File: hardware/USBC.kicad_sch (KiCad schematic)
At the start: 11 parts, among them J20 USB_C_Receptacle_USB2.0_16P, U33 USBLC6-2P6, U8 CP2102N-A02-GQFN20

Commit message: simple changes to the Pulse leds
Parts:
- added D13, D14: LED, LED_SMD:LED_0805_2012Metric, symbol Device:LED
- added R24, R25: 220, symbol Device:R
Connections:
- net GND: now also R24.1, R25.2
- net RXT: now reaches U8.19 (GPIO.3_/_RXT)
- net RXT: now also D14.2 (A)
- net TXT: now reaches U8.20 (GPIO.2_/_TXT)
- net TXT: now also D13.2 (A)
- new net: D14.1 (K), R25.1
- new net: D13.1 (K), R24.2
- no-connect marks 12 -> 10

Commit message: usbc-update
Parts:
- added U11: CDSOT236-0504C, Package_TO_SOT_SMD:SOT-23-6, symbol Power_Protection:CDSOT236-0504C
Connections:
- net 5V_VBUS: now also U11.5 (VP)
- net D_N: now also U11.6 (IO4)
- net D_P: now also U11.4 (IO3)
- net GND: now also U11.2 (VN)
- net CC_ONE: now reaches J20.A5 (CC1), R300.1
- net CC_ONE: now also U11.1 (IO1)
- net CC_TWO: now reaches J20.B5 (CC2), R9.1
- net CC_TWO: now also U11.3 (IO2)
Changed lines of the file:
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@@
+	(wire
+		(pts
+			(xy 99.06 128.27) (xy 102.87 128.27)
+		)
+		(stroke
+			(width 0)
+			(type default)
+		)
+	)
 	(wire
 		(pts
@@
 	(wire
 		(pts
+			(xy 102.87 128.27) (xy 102.87 134.62)
+		)
+		(stroke
+			(width 0)
+			(type default)
+		)
+	)
+	(wire
+		(pts
 			(xy 78.74 76.2) (xy 86.36 76.2)
 		)
@@
 	(wire
 		(pts
+			(xy 64.77 128.27) (xy 73.66 128.27)
+		)
+		(stroke
+			(width 0)
+			(type default)
+		)
+	)
+	(wire
+		(pts
 			(xy 77.47 91.44) (xy 77.47 88.9)
 		)
@@
 			(width 0)
 			(type default)
+		)
+	)
+	(label "CC_TWO"
+		(at 73.66 83.82 0)
+		(effects
+			(font
+				(size 1.27 1.27)
+			)
+			(justify left bottom)
 		)
 	)
@@
 		)
 	)
+	(label "CC_TWO"
+		(at 88.9 140.97 270)
+		(effects
+			(font
+				(size 1.27 1.27)
+			)
+			(justify right bottom)
+		)
+	)
 	(label "RXT"
 		(at 234.95 127 0)
@@
 	)
 	(label "D_N"
+		(at 88.9 115.57 0)
+		(effects
+			(font
+				(size 1.27 1.27)
+			)
+			(justify left bottom)
+		)
+	)
+	(label "D_N"
 		(at 105.41 68.58 180)
 		(effects
@@
 			)
 			(justify right bottom)
+		)
+	)
+	(label "CC_ONE"
+		(at 83.82 140.97 270)
+		(effects
+			(font
+				(size 1.27 1.27)
+			)
+			(justify right bottom)
+		)
+	)
+	(label "CC_ONE"
+		(at 73.66 81.28 0)
+		(effects
+			(font
+				(size 1.27 1.27)
+			)
+			(justify left bottom)
 		)
 	)
 	(label "D_P"
 		(at 73.66 93.98 0)
+		(effects
+			(font
+				(size 1.27 1.27)
+			)
+			(justify left bottom)
+		)
+	)
+	(label "D_P"
+		(at 83.82 115.57 0)
 		(effects
 			(font
@@
 		)
 	)
+	(hierarchical_label "5V_VBUS"
+		(shape output)
+		(at 64.77 128.27 180)
+		(effects
+			(font
+				(size 1.27 1.27)
+			)
+			(justify right)
+		)
+	)
 	(hierarchical_label "BUCK_3.3V"
 		(shape input)
@@
 	)
 	(symbol
+		(lib_id "Power_Protection:CDSOT236-0504C")
+		(at 86.36 128.27 90)
+		(unit 1)
+		(exclude_from_sim no)
+		(in_bom yes)
+		(on_board yes)
+		(dnp no)
+		(fields_autoplaced yes)
+		(property "Reference" "U11"
+			(at 106.68 121.8498 90)
+			(effects
+				(font
+					(size 1.27 1.27)
+				)
+			)
+		)
+		(property "Value" "CDSOT236-0504C"
+			(at 106.68 124.3898 90)
+			(effects
+				(font
+					(size 1.27 1.27)
+				)
+			)
+		)
+		(property "Footprint" "Package_TO_SOT_SMD:SOT-23-6"
+			(at 97.79 110.49 0)
+			(effects
+				(font
+					(size 1.27 1.27)
+				)
+				(hide yes)
+			)
+		)
+		(property "Datasheet" "https://www.bourns.com/docs/product-datasheets/cdsot236-0504c.pdf"
+			(at 86.36 128.27 0)
+			(effects
+				(font
+					(size 1.27 1.27)
+				)
+				(hide yes)
+			)
+		)
+		(property "Description" "Low capacitance ESD diode / steering Diode Array, SOT23-6"
+			(at 86.36 128.27 0)
+			(effects
+				(font
+					(size 1.27 1.27)
+				)
+				(hide yes)
+			)
+		)
+		(pin "3"
+		)
+		(pin "1"
+		)
+		(pin "4"
+		)
+		(pin "5"
+		)
+		(pin "2"
+		)
+		(pin "6"
+		)
+		(instances
+			(project ""
+				(path "/8f5928e8-0fc1-4443-a20f-3bfeb956761e/53a20cc4-87c9-41e2-9c0c-c30bc75df497"
+					(reference "U11")
+					(unit 1)
+				)
+			)
+		)
+	)
+	(symbol
 		(lib_id "Device:R")
 		(at 142.24 127 0)
@@
 					(unit 1)
 				)
+			)
+		)
+	)
+	(symbol
+		(lib_id "power:GND")
+		(at 102.87 134.62 0)
+		(unit 1)
+		(exclude_from_sim no)
+		(in_bom yes)
+		(on_board yes)
+		(dnp no)
+		(fields_autoplaced yes)
+		(property "Reference" "#PWR030"
+			(at 102.87 140.97 0)
+			(effects
+				(font
+					(size 1.27 1.27)
+				)
+				(hide yes)
+			)
+		)
+		(property "Value" "GND"
+			(at 102.87 139.7 0)
+			(effects
+				(font
+					(size 1.27 1.27)
+				)
+			)
+		)
+		(property "Footprint" ""
+			(at 102.87 134.62 0)
+			(effects
+				(font
+					(size 1.27 1.27)
+				)
+				(hide yes)
+			)
+		)
+		(property "Datasheet" ""
+			(at 102.87 134.62 0)
+			(effects
+				(font
+					(size 1.27 1.27)
+				)
+				(hide yes)
+			)
+		)
+		(property "Description" "Power symbol creates a global label with name \"GND\" , ground"
+			(at 102.87 134.62 0)
+			(effects
+				(font
+					(size 1.27 1.27)
+				)
+				(hide yes)
+			)
+		)
+		(pin "1"
+		)
+		(instances
+			(project ""
+				(path "/8f5928e8-0fc1-4443-a20f-3bfeb956761e/53a20cc4-87c9-41e2-9c0c-c30bc75df497"
+					(reference "#PWR030")
+					(unit 1)
+				)

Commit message: Debugging LED added
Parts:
- R14, R26, R27, R28, R300, R9: footprint Resistor_SMD:R_0603_1608Metric -> Resistor_SMD:R_0805_2012Metric
- R24, R25: footprint (none) -> Resistor_SMD:R_0805_2012Metric
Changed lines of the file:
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@@
 			)
 		)
-		(property "Footprint" ""
+		(property "Footprint" "Resistor_SMD:R_0805_2012Metric"
 			(at 233.172 142.24 90)
 			(effects
@@
 			)
 		)
-		(property "Footprint" "Resistor_SMD:R_0603_1608Metric"
+		(property "Footprint" "Resistor_SMD:R_0805_2012Metric"
 			(at 85.09 83.058 90)
 			(effects
@@
 			)
 		)
-		(property "Footprint" "Resistor_SMD:R_0603_1608Metric"
+		(property "Footprint" "Resistor_SMD:R_0805_2012Metric"
 			(at 154.432 116.84 90)
 			(effects
@@
 			)
 		)
-		(property "Footprint" "Resistor_SMD:R_0603_1608Metric"
+		(property "Footprint" "Resistor_SMD:R_0805_2012Metric"
 			(at 140.462 116.84 90)
 			(effects
@@
 			)
 		)
-		(property "Footprint" "Resistor_SMD:R_0603_1608Metric"
+		(property "Footprint" "Resistor_SMD:R_0805_2012Metric"
 			(at 85.09 85.598 90)
 			(effects
@@
 			)
 		)
-		(property "Footprint" ""
+		(property "Footprint" "Resistor_SMD:R_0805_2012Metric"
 			(at 227.838 142.24 90)
 			(effects
@@
 			)
 		)
-		(property "Footprint" "Resistor_SMD:R_0603_1608Metric"
+		(property "Footprint" "Resistor_SMD:R_0805_2012Metric"
 			(at 140.462 127 90)
 			(effects
@@
 			)
 		)
-		(property "Footprint" "Resistor_SMD:R_0603_1608Metric"
+		(property "Footprint" "Resistor_SMD:R_0805_2012Metric"
 			(at 47.752 116.84 90)
 			(effects

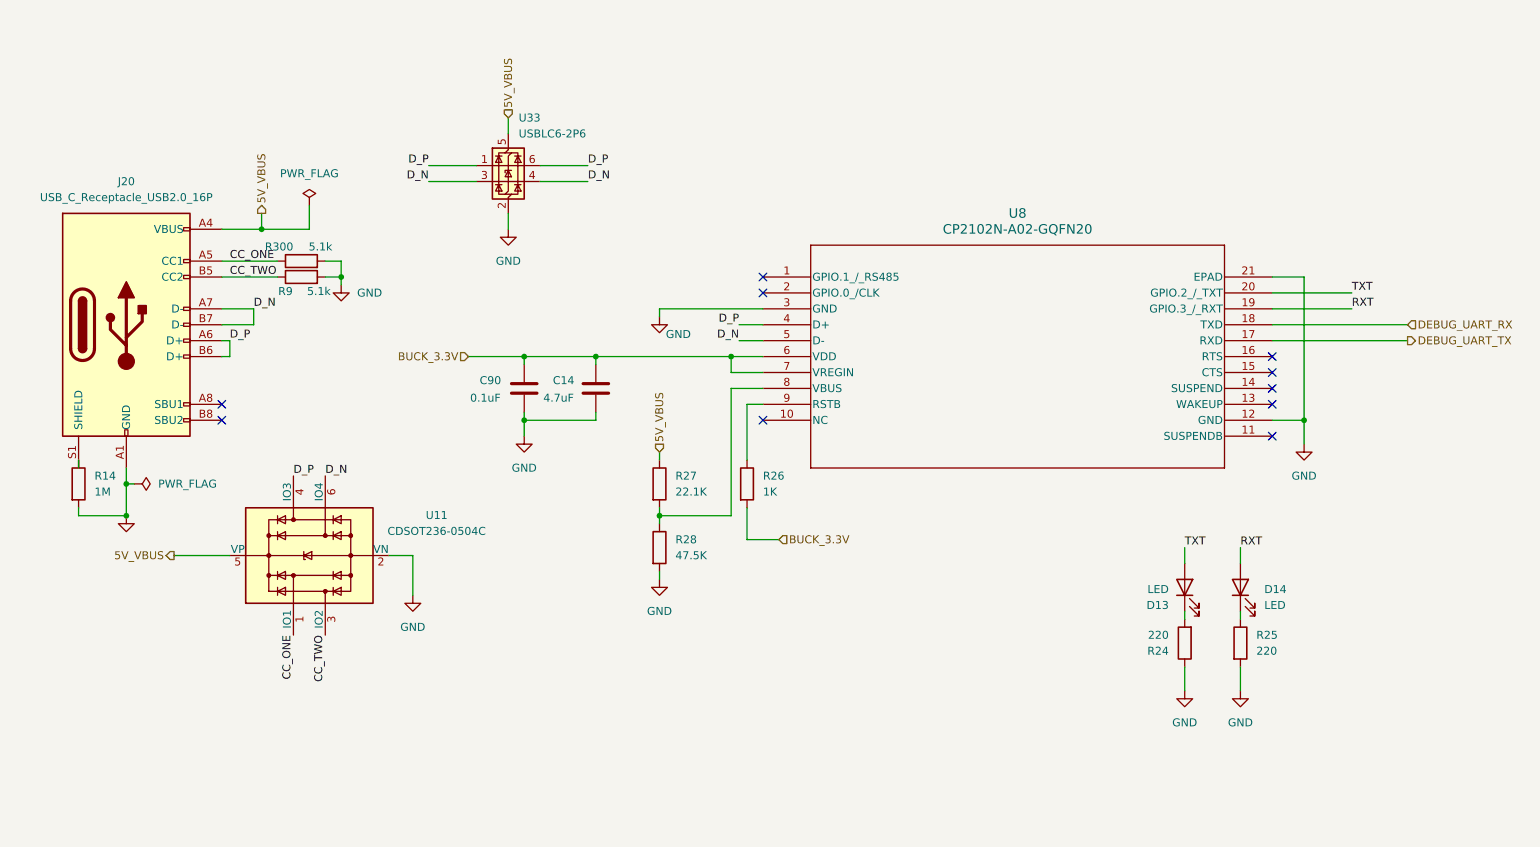
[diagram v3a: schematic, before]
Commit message: Fixed MCU JTAG/Reordered pages
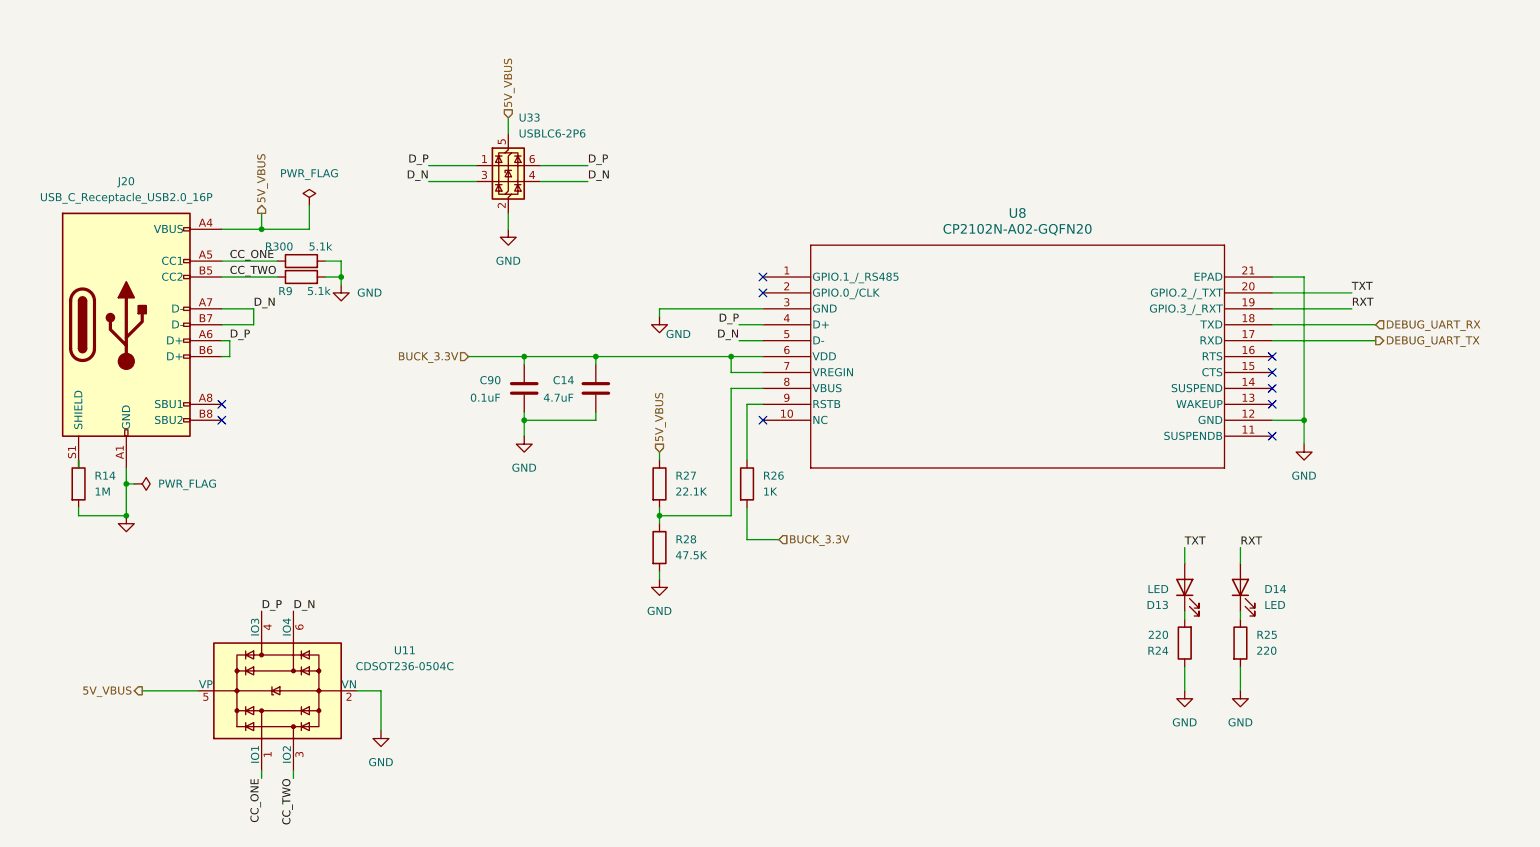
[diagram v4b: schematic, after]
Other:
- moved on the sheet: U11
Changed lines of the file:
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@@
+	(wire
+		(pts
+			(xy 78.74 163.83) (xy 78.74 162.56)
+		)
+		(stroke
+			(width 0)
+			(type default)
+		)
+	)
 	(wire
 		(pts
@@
 	(wire
 		(pts
-			(xy 240.03 91.44) (xy 261.62 91.44)
+			(xy 240.03 91.44) (xy 256.54 91.44)
 		)
 		(stroke
@@
 	(wire
 		(pts
-			(xy 240.03 93.98) (xy 261.62 93.98)
+			(xy 240.03 93.98) (xy 256.54 93.98)
 		)
 		(stroke
@@
 	(wire
 		(pts
-			(xy 99.06 128.27) (xy 102.87 128.27)
+			(xy 93.98 149.86) (xy 97.79 149.86)
 		)
 		(stroke
@@
 	(wire
 		(pts
-			(xy 102.87 128.27) (xy 102.87 134.62)
+			(xy 97.79 149.86) (xy 97.79 156.21)
 		)
 		(stroke
@@
 	(wire
 		(pts
+			(xy 83.82 163.83) (xy 83.82 162.56)
+		)
+		(stroke
+			(width 0)
+			(type default)
+		)
+	)
+	(wire
+		(pts
 			(xy 72.39 91.44) (xy 77.47 91.44)
 		)
@@
 	(wire
 		(pts
-			(xy 64.77 128.27) (xy 73.66 128.27)
+			(xy 59.69 149.86) (xy 68.58 149.86)
 		)
 		(stroke
@@
 	)
 	(label "CC_TWO"
-		(at 88.9 140.97 270)
+		(at 83.82 163.83 270)
 		(effects
 			(font
@@
 	)
 	(label "D_N"
-		(at 88.9 115.57 0)
+		(at 83.82 137.16 0)
 		(effects
 			(font
@@
 	)
 	(label "CC_ONE"
-		(at 83.82 140.97 270)
+		(at 78.74 163.83 270)
 		(effects
 			(font
@@
 	)
 	(label "D_P"
-		(at 83.82 115.57 0)
+		(at 78.74 137.16 0)
 		(effects
 			(font
@@
 	(hierarchical_label "DEBUG_UART_RX"
 		(shape input)
-		(at 261.62 91.44 0)
+		(at 256.54 91.44 0)
 		(effects
 			(font
@@
 	(hierarchical_label "DEBUG_UART_TX"
 		(shape output)
-		(at 261.62 93.98 0)
+		(at 256.54 93.98 0)
 		(effects
 			(font
@@
 	(hierarchical_label "5V_VBUS"
 		(shape output)
-		(at 64.77 128.27 180)
+		(at 59.69 149.86 180)
 		(effects
 			(font
@@
 	(symbol
 		(lib_id "Power_Protection:CDSOT236-0504C")
-		(at 86.36 128.27 90)
+		(at 81.28 149.86 90)
 		(unit 1)
 		(exclude_from_sim no)
@@
 		(fields_autoplaced yes)
 		(property "Reference" "U11"
-			(at 106.68 121.8498 90)
+			(at 101.6 143.4398 90)
 			(effects
 				(font
@@
 		)
 		(property "Value" "CDSOT236-0504C"
-			(at 106.68 124.3898 90)
+			(at 101.6 145.9798 90)
 			(effects
 				(font
@@
 		)
 		(property "Footprint" "Package_TO_SOT_SMD:SOT-23-6"
-			(at 97.79 110.49 0)
+			(at 92.71 132.08 0)
 			(effects
 				(font
@@
 		)
 		(property "Datasheet" "https://www.bourns.com/docs/product-datasheets/cdsot236-0504c.pdf"
-			(at 86.36 128.27 0)
+			(at 81.28 149.86 0)
 			(effects
 				(font
@@
 		)
 		(property "Description" "Low capacitance ESD diode / steering Diode Array, SOT23-6"
-			(at 86.36 128.27 0)
+			(at 81.28 149.86 0)
 			(effects
 				(font
@@
 	(symbol
 		(lib_id "power:GND")
-		(at 102.87 134.62 0)
+		(at 97.79 156.21 0)
 		(unit 1)
 		(exclude_from_sim no)
@@
 		(fields_autoplaced yes)
 		(property "Reference" "#PWR030"
-			(at 102.87 140.97 0)
+			(at 97.79 162.56 0)
 			(effects
 				(font
@@
 		)
 		(property "Value" "GND"
-			(at 102.87 139.7 0)
+			(at 97.79 161.29 0)
 			(effects
 				(font
@@
 		)
 		(property "Footprint" ""
-			(at 102.87 134.62 0)
+			(at 97.79 156.21 0)
 			(effects
 				(font
@@
 		)
 		(property "Datasheet" ""
-			(at 102.87 134.62 0)
+			(at 97.79 156.21 0)
 			(effects
 				(font
@@
 		)
 		(property "Description" "Power symbol creates a global label with name \"GND\" , ground"
-			(at 102.87 134.62 0)
-			(effects
-				(font
+			(at 97.79 156.21 0)
+			(effects
+				(font

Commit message: cleanup
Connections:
- net CC_ONE renamed CC1
- net CC_TWO renamed CC2
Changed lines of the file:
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@@
 		)
 	)
-	(label "CC_TWO"
+	(label "CC2"
 		(at 73.66 83.82 0)
 		(effects
@@
 		)
 	)
-	(label "CC_TWO"
+	(label "CC2"
 		(at 83.82 163.83 270)
 		(effects
@@
 		)
 	)
-	(label "CC_ONE"
+	(label "CC1"
 		(at 78.74 163.83 270)
 		(effects
@@
 		)
 	)
-	(label "CC_ONE"
+	(label "CC1"
 		(at 73.66 81.28 0)
 		(effects
@@
 		(dnp no)
 		(property "Reference" "R300"
-			(at 81.534 78.994 90)
-			(effects
-				(font
+			(at 82.55 78.486 90)
+			(effects
+				(font

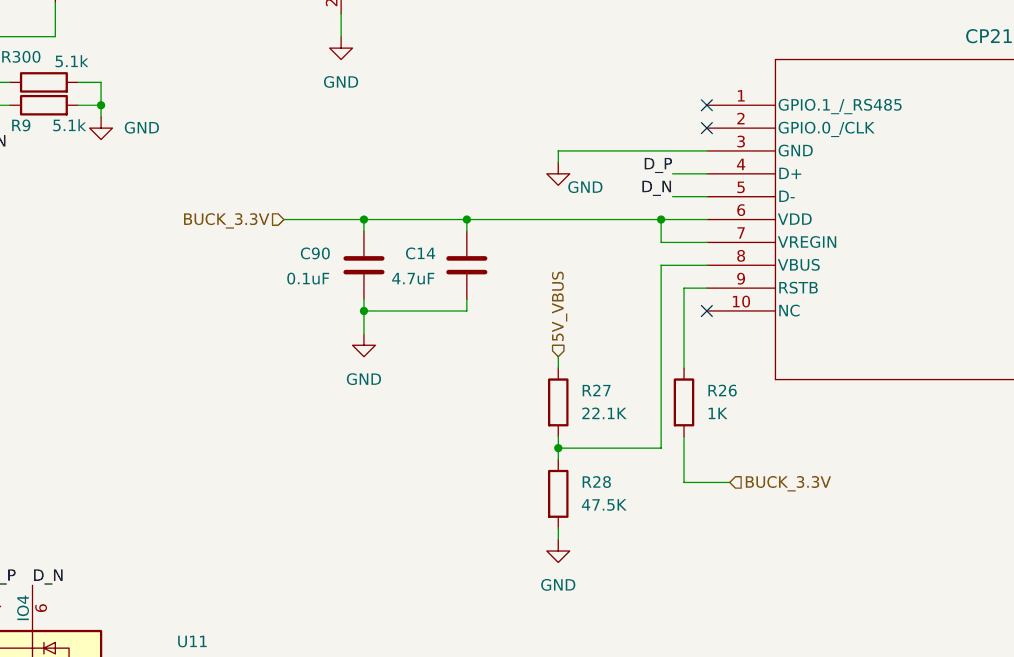
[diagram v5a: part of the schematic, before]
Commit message: Replaced 3.3V symbol
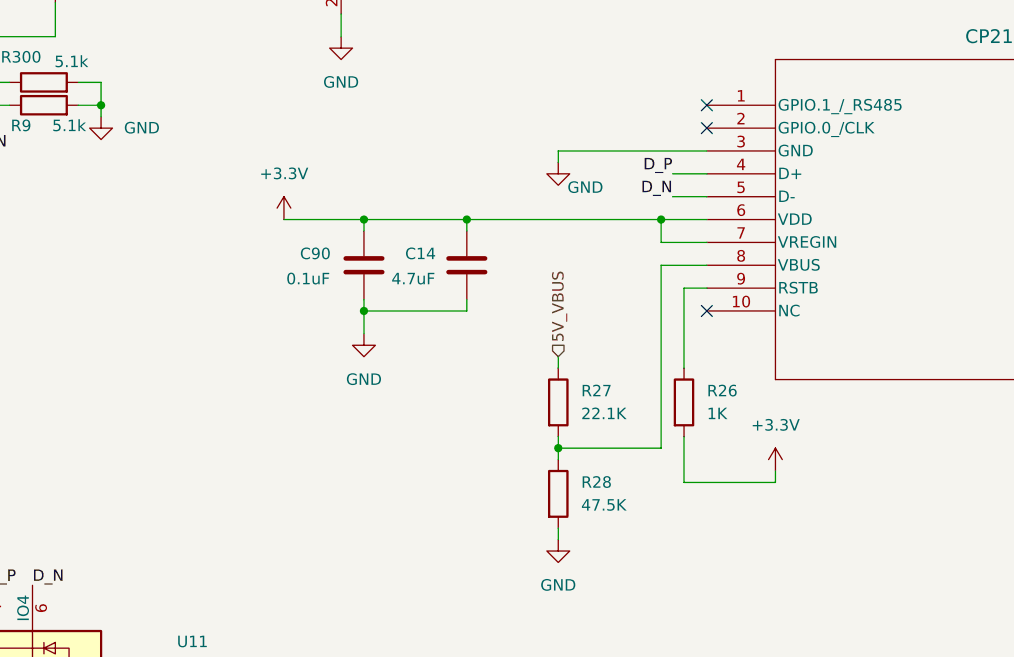
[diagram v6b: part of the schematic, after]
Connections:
- net BUCK_3.3V renamed +3.3V
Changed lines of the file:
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@@
 	(wire
 		(pts
-			(xy 156.21 125.73) (xy 161.29 125.73)
+			(xy 156.21 125.73) (xy 166.37 125.73)
 		)
 		(stroke
@@
 		(pts
 			(xy 240.03 93.98) (xy 256.54 93.98)
+		)
+		(stroke
+			(width 0)
+			(type default)
+		)
+	)
+	(wire
+		(pts
+			(xy 166.37 125.73) (xy 166.37 124.46)
 		)
 		(stroke
@@
 			)
 			(justify right bottom)
-		)
-	)
-	(hierarchical_label "BUCK_3.3V"
-		(shape input)
-		(at 161.29 125.73 0)
-		(effects
-			(font
-				(size 1.27 1.27)
-			)
-			(justify left)
 		)
 	)
@@
 		)
 	)
-	(hierarchical_label "BUCK_3.3V"
-		(shape input)
-		(at 111.76 96.52 180)
-		(effects
-			(font
-				(size 1.27 1.27)
-			)
-			(justify right)
-		)
-	)
 	(hierarchical_label "5V_VBUS"
 		(shape input)
@@
 	)
 	(symbol
+		(lib_id "power:+3.3V")
+		(at 111.76 96.52 0)
+		(unit 1)
+		(exclude_from_sim no)
+		(in_bom yes)
+		(on_board yes)
+		(dnp no)
+		(fields_autoplaced yes)
+		(property "Reference" "#PWR079"
+			(at 111.76 100.33 0)
+			(effects
+				(font
+					(size 1.27 1.27)
+				)
+				(hide yes)
+			)
+		)
+		(property "Value" "+3.3V"
+			(at 111.76 91.44 0)
+			(effects
+				(font
+					(size 1.27 1.27)
+				)
+			)
+		)
+		(property "Footprint" ""
+			(at 111.76 96.52 0)
+			(effects
+				(font
+					(size 1.27 1.27)
+				)
+				(hide yes)
+			)
+		)
+		(property "Datasheet" ""
+			(at 111.76 96.52 0)
+			(effects
+				(font
+					(size 1.27 1.27)
+				)
+				(hide yes)
+			)
+		)
+		(property "Description" "Power symbol creates a global label with name \"+3.3V\""
+			(at 111.76 96.52 0)
+			(effects
+				(font
+					(size 1.27 1.27)
+				)
+				(hide yes)
+			)
+		)
+		(pin "1"
+		)
+		(instances
+			(project "Senior_Design"
+				(path "/8f5928e8-0fc1-4443-a20f-3bfeb956761e/53a20cc4-87c9-41e2-9c0c-c30bc75df497"
+					(reference "#PWR079")
+					(unit 1)
+				)
+			)
+		)
+	)
+	(symbol
 		(lib_id "Device:R")
 		(at 85.09 81.28 90)
@@
 					(unit 1)
 				)
+			)
+		)
+	)
+	(symbol
+		(lib_id "power:+3.3V")
+		(at 166.37 124.46 0)
+		(unit 1)
+		(exclude_from_sim no)
+		(in_bom yes)
+		(on_board yes)
+		(dnp no)
+		(fields_autoplaced yes)
+		(property "Reference" "#PWR080"
+			(at 166.37 128.27 0)
+			(effects
+				(font
+					(size 1.27 1.27)
+				)
+				(hide yes)
+			)
+		)
+		(property "Value" "+3.3V"
+			(at 166.37 119.38 0)
+			(effects
+				(font
+					(size 1.27 1.27)
+				)
+			)
+		)
+		(property "Footprint" ""
+			(at 166.37 124.46 0)
+			(effects
+				(font
+					(size 1.27 1.27)
+				)
+				(hide yes)
+			)
+		)
+		(property "Datasheet" ""
+			(at 166.37 124.46 0)
+			(effects
+				(font
+					(size 1.27 1.27)
+				)
+				(hide yes)
+			)
+		)
+		(property "Description" "Power symbol creates a global label with name \"+3.3V\""
+			(at 166.37 124.46 0)
+			(effects
+				(font
+					(size 1.27 1.27)
+				)
+				(hide yes)
+			)
+		)
+		(pin "1"
+		)
+		(instances
+			(project "Senior_Design"
+				(path "/8f5928e8-0fc1-4443-a20f-3bfeb956761e/53a20cc4-87c9-41e2-9c0c-c30bc75df497"
+					(reference "#PWR080")
+					(unit 1)
+				)
